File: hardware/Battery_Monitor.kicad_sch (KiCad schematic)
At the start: 3 parts

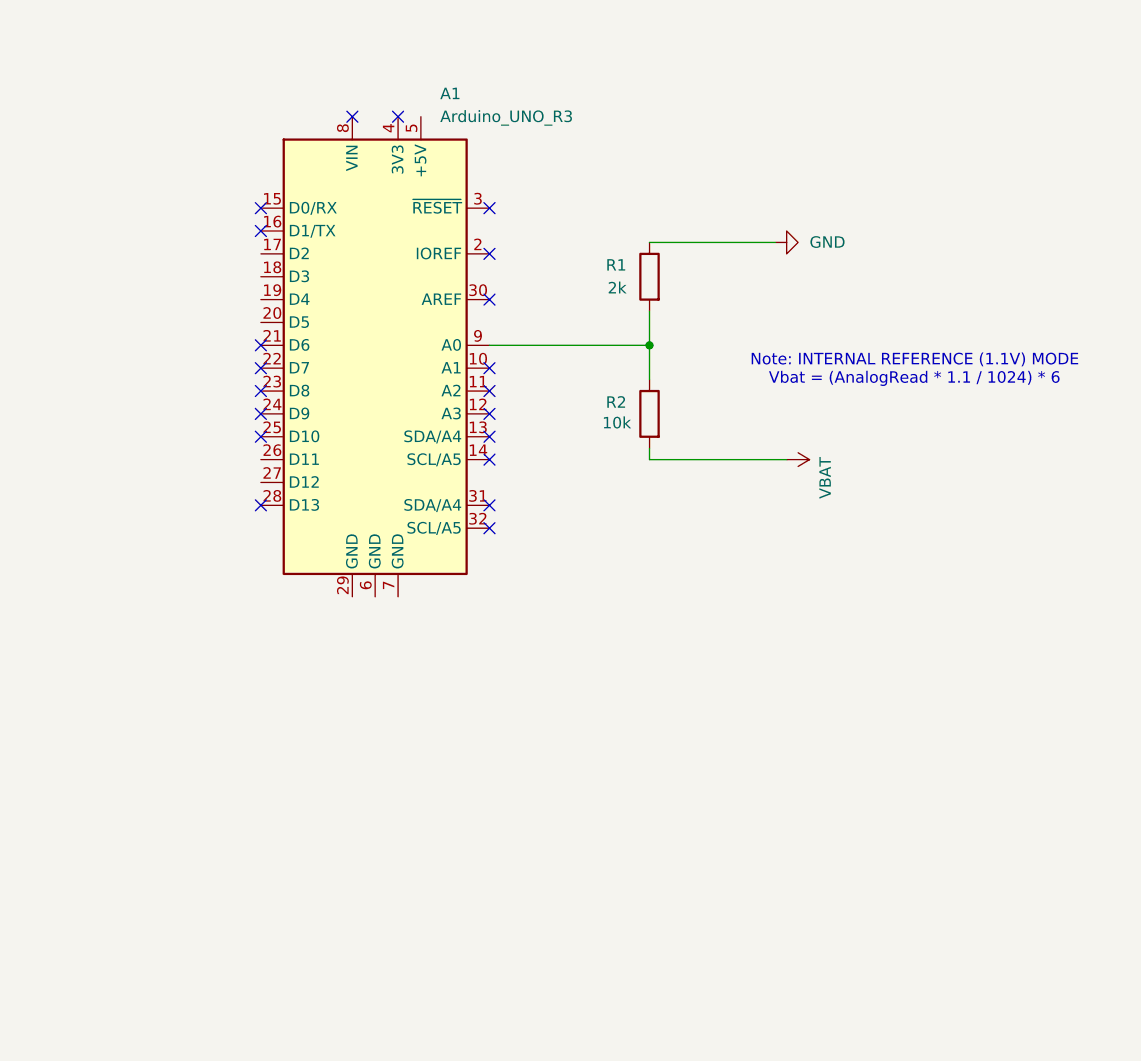
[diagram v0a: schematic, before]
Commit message: Fix: Remove embedded git repository and clean up ignore list
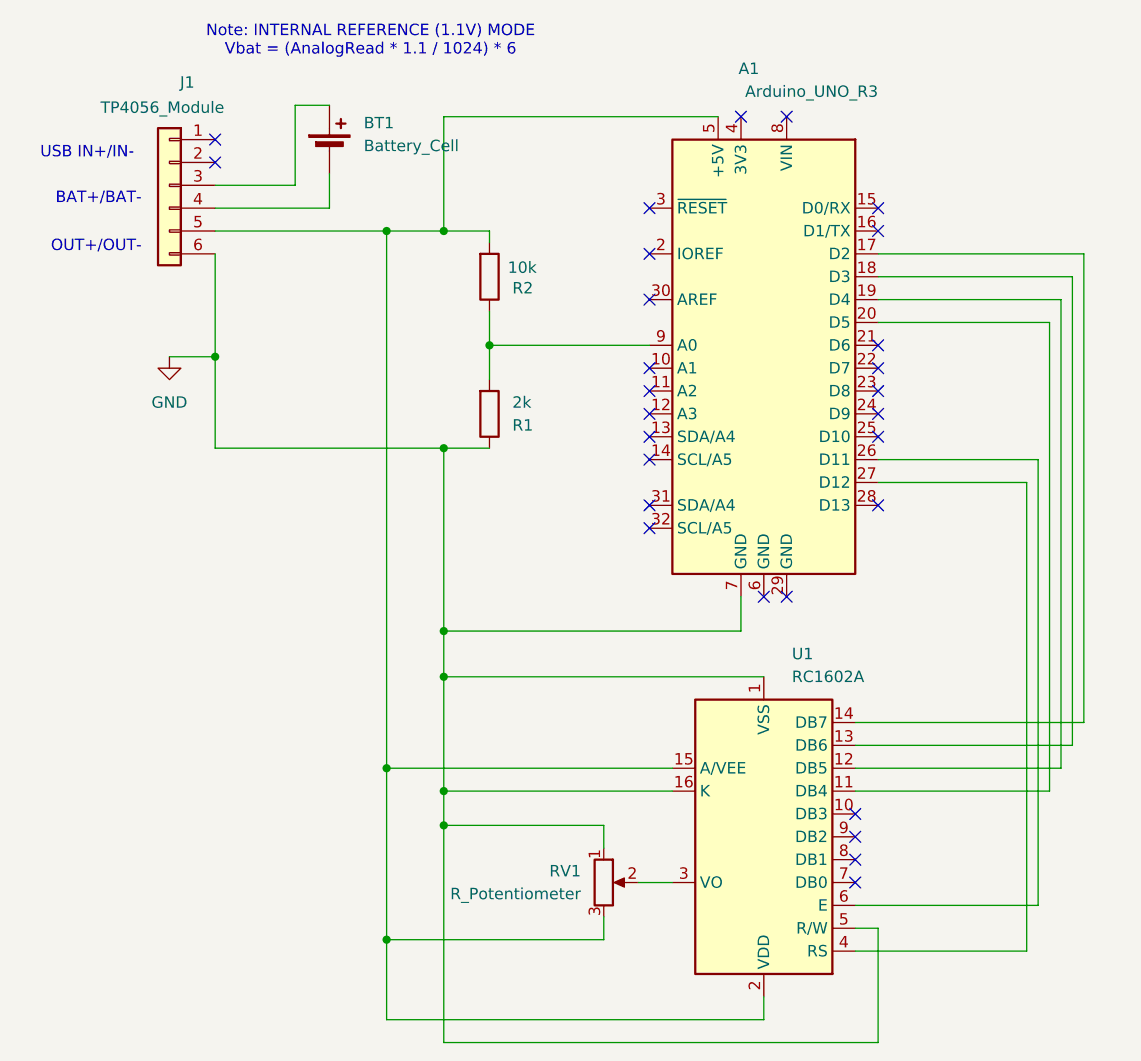
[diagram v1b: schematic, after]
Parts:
- added BT1: Battery_Cell, symbol Device:Battery_Cell
- added J1: TP4056_Module, symbol Connector_Generic:Conn_01x06
- added RV1: R_Potentiometer, symbol Device:R_Potentiometer
- added U1: RC1602A, Display:RC1602A, symbol Display_Character:RC1602A
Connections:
- net VBAT is gone; now on an unnamed net: R2.2
- net GND: now also A1.7 (GND), J1.6 (Pin_6), RV1.1, U1.1 (VSS), U1.16 (K), U1.5 (R/W)
- net at A1.17 (D2): now also U1.14 (DB7)
- net at A1.18 (D3): now also U1.13 (DB6)
- net at A1.19 (D4): now also U1.12 (DB5)
- net at A1.20 (D5): now also U1.11 (DB4)
- net at A1.26 (D11): now also U1.6 (E)
- net at A1.27 (D12): now also U1.4 (RS)
- net at A1.5 (+5V): now also J1.5 (Pin_5), RV1.3, U1.15 (A/VEE), U1.2 (VDD)
- new net: BT1.1 (+), J1.3 (Pin_3)
- new net: BT1.2 (-), J1.4 (Pin_4)
- new net: RV1.2, U1.3 (VO)
- no-connect marks 20 -> 28
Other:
- note added: "BAT+/BAT-"
- note added: "OUT+/OUT-"
- note added: "USB IN+/IN-"
- moved on the sheet: A1, R1, R2
